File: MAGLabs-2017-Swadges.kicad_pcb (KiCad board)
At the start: 2 copper layers, 70 x 120 mm, 34 parts, among them J1 LCD Screen, J2 Valve Magic, J3 Program, U1 ESP12E

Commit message: Update design
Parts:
- moved C3 44.6 mm to (128.5, 38.0), turned to 270 degrees
- moved C4 37.7 mm to (153.0, 109.8)
- moved C2 25.3 mm to (118.6, 105.6), turned to 0 degrees
- moved R2 19.6 mm to (124.4, 107.6)
- moved R3 6.45 mm to (148.4, 112.0)
- moved C1 4.01 mm to (127.0, 82.8)
- moved R5 1.55 mm to (143.4, 112.0)
- moved R4 1.40 mm to (145.1, 112.0)
- moved R6 1.25 mm to (146.8, 112.0)
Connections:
- R2 pad 2: (no net) -> Net-(R2-Pad2)
- R3 pad 2: (no net) -> GPIO0
- S8 pad 1: Net-(S8-Pad1) -> Net-(R2-Pad2)
- U1 pad 17: Net-(S8-Pad1) -> Net-(R2-Pad2)
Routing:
- net Net-(BT1-Pad2): track 81.7 -> 165.8 mm
- net Net-(R2-Pad2): track 0.00 -> 71.9 mm
- net Net-(S8-Pad1): track 67.0 -> 0.00 mm
- net +3V3: track 309.2 -> 366.6 mm, vias 2 -> 9
- net GND: track 366.9 -> 378.1 mm, vias 16 -> 18
- net Net-(R5-Pad2): track 20.1 -> 15.2 mm, vias 0 -> 2
- net Net-(D1-Pad2): track 35.3 -> 31.7 mm
- net Net-(R6-Pad2): track 41.2 -> 39.4 mm
- net GPIO0: track 110.6 -> 112.1 mm, vias 2 -> 3

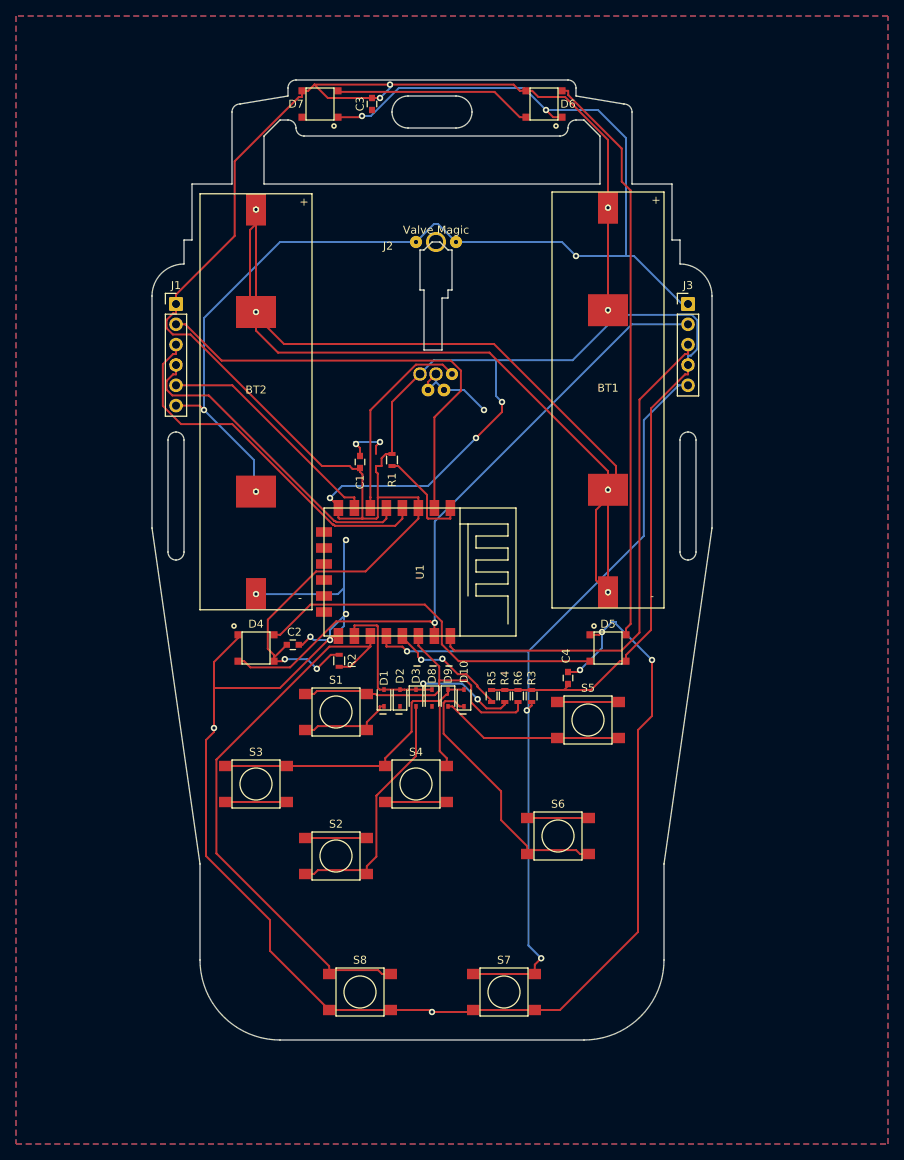
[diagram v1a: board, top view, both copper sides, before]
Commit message: Fixed diodes
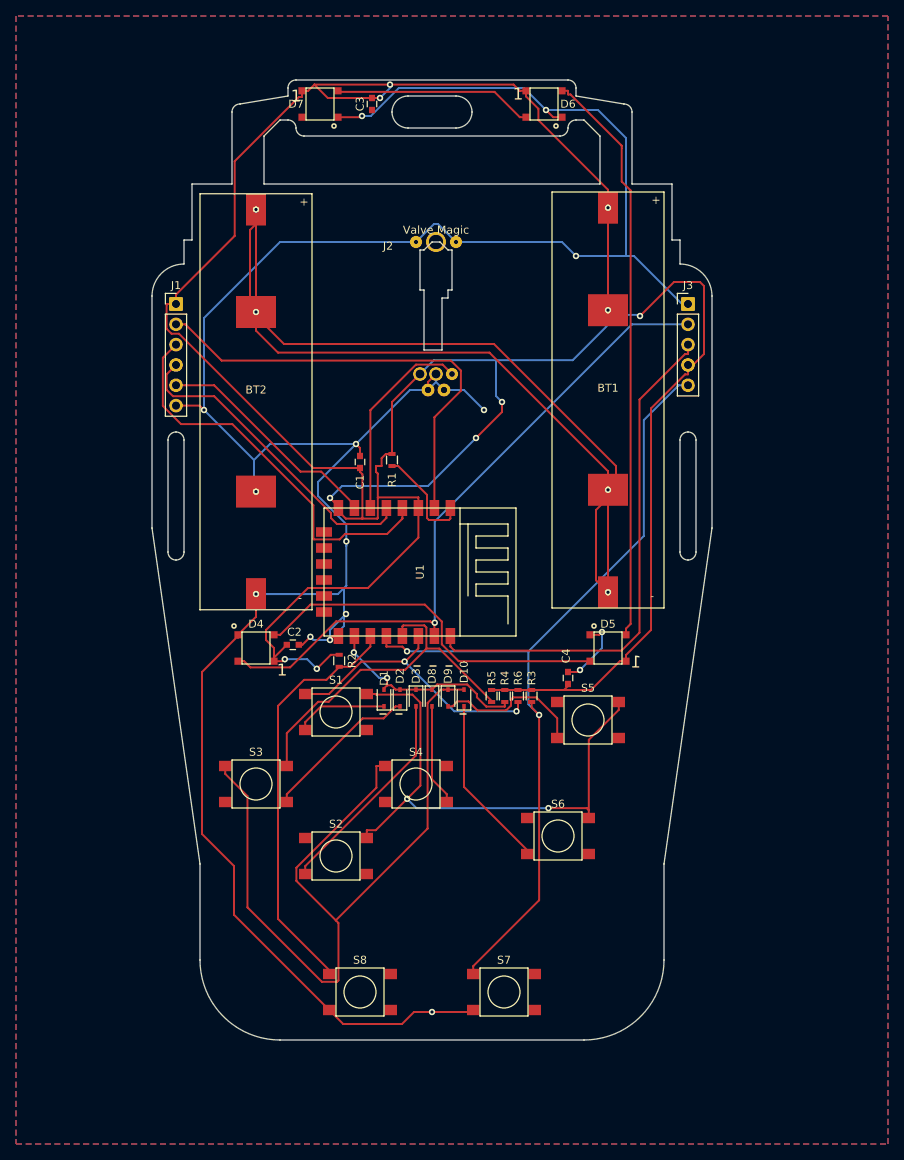
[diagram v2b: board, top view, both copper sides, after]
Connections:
- D2 pad 1: (no net) -> Net-(D2-Pad1)
- D7 pad 2: (no net) -> Net-(D7-Pad2)
- D8 pad 2: (no net) -> Net-(D8-Pad2)
- U1 pad 10: (no net) -> Net-(U1-Pad10)
- U1 pad 11: (no net) -> Net-(U1-Pad11)
- U1 pad 12: (no net) -> Net-(U1-Pad12)
- U1 pad 13: (no net) -> Net-(U1-Pad13)
- U1 pad 14: (no net) -> Net-(U1-Pad14)
- U1 pad 9: (no net) -> Net-(U1-Pad9)
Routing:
- net Net-(S1-Pad2): track 0.00 -> 67.2 mm, vias 0 -> 2
- net Net-(D10-Pad2): track 45.4 -> 105.5 mm
- net GND: track 378.1 -> 336.0 mm, vias 18 -> 15
- net Net-(R5-Pad2): track 15.2 -> 44.1 mm, vias 2 -> 0
- net Net-(R2-Pad2): track 71.9 -> 52.1 mm
- net Net-(D2-Pad1): track 0.00 -> 19.7 mm
- net Net-(D8-Pad2): track 0.00 -> 12.7 mm
- net Net-(D10-Pad1): track 34.0 -> 21.7 mm
- net Net-(S6-Pad1): track 7.70 -> 0.00 mm
- net Net-(S5-Pad1): track 7.70 -> 0.00 mm
- net Net-(S4-Pad3): track 7.70 -> 0.00 mm
- net Net-(S3-Pad3): track 7.70 -> 0.00 mm
- net Net-(S2-Pad1): track 7.70 -> 0.00 mm
- net +3V3: track 366.6 -> 372.6 mm, vias 9 -> 10
- net Net-(D1-Pad2): track 31.7 -> 26.3 mm
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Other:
- net class Default: clearance 0.2 -> 0.196
- rule trace_clearance: 0.2 -> 0.196
- board text added: "1"

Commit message: Update design
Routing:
- net GND: track 336.0 -> 373.8 mm, vias 15 -> 19
- net (no net): track 0.00 -> 1.51 mm
- net Net-(BT1-Pad2): track 165.8 -> 167.3 mm
- net +3V3: track 372.6 -> 371.8 mm

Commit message: Added button labels
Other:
- board text added: "A"
- board text added: "B"
- board text added: "LCD Screen"
- board text added: "Program"
- board text added: "SELECT"
- board text added: "START/PROGRAM"
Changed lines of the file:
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@@
-(kicad_pcb (version 4) (host pcbnew 4.0.6-e0-6349~53~ubuntu16.04.1)
+(kicad_pcb (version 20170123) (host pcbnew "(2017-07-14 revision d3b382c28)-master")
   (general
-    (links 80)
-    (no_connects 0)
-    (area 84 27 193.000001 168.000001)
     (thickness 1.6)
-    (drawings 88)
+    (drawings 107)
     (tracks 519)
     (zones 0)
@@
     (47 F.CrtYd user)
     (48 B.Fab user)
-    (49 F.Fab user hide)
+    (49 F.Fab user)
   )
   (setup
@@
     (visible_elements FFFFEFFF)
     (pcbplotparams
-      (layerselection 0x010f8_80000001)
+      (layerselection 0x010f8_ffffffff)
       (usegerberextensions true)
       (excludeedgelayer true)
@@
       (hpglpenspeed 20)
       (hpglpendiameter 15)
-      (hpglpenoverlay 2)
       (psnegative false)
       (psa4output false)
@@
     (at 145 149)
     (attr smd)
-    (fp_text reference S7 (at 0 -4) (layer F.SilkS)
+    (fp_text reference S7 (at 0 4) (layer F.SilkS)
       (effects (font (size 1 1) (thickness 0.15)))
     )
@@
     (at 127 149)
     (attr smd)
-    (fp_text reference S8 (at 0 -4) (layer F.SilkS)
+    (fp_text reference S8 (at 0 4) (layer F.SilkS)
       (effects (font (size 1 1) (thickness 0.15)))
     )
@@
     (at 124 132)
     (attr smd)
-    (fp_text reference S2 (at 0 -4) (layer F.SilkS)
+    (fp_text reference S2 (at 0 4) (layer F.SilkS)
       (effects (font (size 1 1) (thickness 0.15)))
     )
@@
       (effects (font (size 1 1) (thickness 0.15)))
     )
-    (fp_text value 0.1u (at -1.75 2.25 360) (layer F.Fab)
+    (fp_text value 0.1u (at -1.75 2.25) (layer F.Fab)
       (effects (font (size 1 1) (thickness 0.15)))
     )
@@
     )
   )
+  (gr_text Program (at 170 68 90) (layer F.SilkS)
+    (effects (font (size 1 1) (thickness 0.2)))
+  )
+  (gr_text "LCD Screen" (at 102 69.5 90) (layer F.SilkS)
+    (effects (font (size 1 1) (thickness 0.2)))
+  )
+  (gr_text A (at 155.5 120) (layer F.SilkS)
+    (effects (font (size 3 3) (thickness 0.3)))
+  )
+  (gr_text B (at 152 135) (layer F.SilkS)
+    (effects (font (size 3 3) (thickness 0.3)))
+  )
+  (gr_text START/PROGRAM (at 145 144) (layer F.SilkS)
+    (effects (font (size 1.5 1.5) (thickness 0.3)))
+  )
+  (gr_text SELECT (at 127 144) (layer F.SilkS)
+    (effects (font (size 1.5 1.5) (thickness 0.3)))
+  )
+  (gr_line (start 120 125) (end 118 123) (angle 90) (layer F.SilkS) (width 0.2))
+  (gr_line (start 120 124) (end 120 125) (angle 90) (layer F.SilkS) (width 0.2))
+  (gr_line (start 120 121) (end 120 124) (angle 90) (layer F.SilkS) (width 0.2))
+  (gr_line (start 118 123) (end 120 121) (angle 90) (layer F.SilkS) (width 0.2))
+  (gr_line (start 126 126) (end 124 128) (angle 90) (layer F.SilkS) (width 0.2))
+  (gr_line (start 122 126) (end 126 126) (angle 90) (layer F.SilkS) (width 0.2))
+  (gr_line (start 124 128) (end 122 126) (angle 90) (layer F.SilkS) (width 0.2))
+  (gr_line (start 128 125) (end 130 123) (angle 90) (layer F.SilkS) (width 0.2))
+  (gr_line (start 128 121) (end 128 125) (angle 90) (layer F.SilkS) (width 0.2))
+  (gr_line (start 130 123) (end 128 121) (angle 90) (layer F.SilkS) (width 0.2))
+  (gr_line (start 126 120) (end 124 118) (angle 90) (layer F.SilkS) (width 0.2))
+  (gr_line (start 122 120) (end 126 120) (angle 90) (layer F.SilkS) (width 0.2))
+  (gr_line (start 124 118) (end 122 120) (angle 90) (layer F.SilkS) (width 0.2))
   (gr_text 1 (at 146.75 36.75) (layer F.SilkS)
     (effects (font (size 1.5 1.5) (thickness 0.3)))

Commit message: Updates
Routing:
- net +3V3: track 371.8 -> 374.2 mm
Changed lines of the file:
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@@
     (thickness 1.6)
     (drawings 107)
-    (tracks 519)
+    (tracks 518)
     (zones 0)
     (modules 34)
@@
   (segment (start 159 85.225) (end 158 86.225) (width 0.25) (layer F.Cu) (net 1))
   (segment (start 114 64) (end 114 64.5) (width 0.25) (layer F.Cu) (net 1))
+  (segment (start 158 50.965) (end 158 42.5) (width 0.25) (layer F.Cu) (net 2) (status 400000))
+  (segment (start 148.9 37.5) (end 147.75 36.35) (width 0.25) (layer F.Cu) (net 2) (status 800000))
+  (segment (start 153 37.5) (end 148.9 37.5) (width 0.25) (layer F.Cu) (net 2))
+  (segment (start 158 42.5) (end 153 37.5) (width 0.25) (layer F.Cu) (net 2))
   (segment (start 146.49996 35.87496) (end 131.340125 35.87496) (width 0.25) (layer F.Cu) (net 2))
+  (segment (start 146.975 36.35) (end 146.49996 35.87496) (width 0.25) (layer F.Cu) (net 2))
+  (segment (start 131.340125 35.87496) (end 130.77444 35.87496) (width 0.25) (layer F.Cu) (net 2))
   (segment (start 147.75 36.35) (end 146.975 36.35) (width 0.25) (layer F.Cu) (net 2))
   (segment (start 129.5 37.25) (end 130.77444 35.97556) (width 0.25) (layer B.Cu) (net 2))
   (segment (start 130.77444 35.97556) (end 130.77444 35.87496) (width 0.25) (layer B.Cu) (net 2))
-  (segment (start 131.340125 35.87496) (end 130.77444 35.87496) (width 0.25) (layer F.Cu) (net 2))
   (segment (start 130.208755 35.87496) (end 130.77444 35.87496) (width 0.25) (layer F.Cu) (net 2))
   (via (at 130.77444 35.87496) (size 0.8) (drill 0.4) (layers F.Cu B.Cu) (net 2))
-  (segment (start 146.975 36.35) (end 146.49996 35.87496) (width 0.25) (layer F.Cu) (net 2))
   (segment (start 129.908495 35.5747) (end 130.208755 35.87496) (width 0.25) (layer F.Cu) (net 2))
   (segment (start 121.301 35.5747) (end 129.908495 35.5747) (width 0.25) (layer F.Cu) (net 2))
@@
   (segment (start 126.375 83.5) (end 127 83.5) (width 0.25) (layer F.Cu) (net 2))
   (segment (start 121.159002 83.5) (end 126.375 83.5) (width 0.25) (layer F.Cu) (net 2))
-  (segment (start 149.301 40.016) (end 158 48.715) (width 0.25) (layer F.Cu) (net 2))
-  (segment (start 149.301 38.601) (end 149.301 40.016) (width 0.25) (layer F.Cu) (net 2))
-  (segment (start 147.75 37.05) (end 149.301 38.601) (width 0.25) (layer F.Cu) (net 2))
-  (segment (start 158 48.715) (end 158 50.965) (width 0.25) (layer F.Cu) (net 2))
-  (segment (start 147.75 36.35) (end 147.75 37.05) (width 0.25) (layer F.Cu) (net 2))
   (via (at 121.6 108.6) (size 0.8) (layers F.Cu B.Cu) (net 2))
   (via (at 117.6 107.4) (size 0.8) (layers F.Cu B.Cu) (net 2))
@@
     (min_thickness 0.254)
     (keepout (tracks not_allowed) (vias not_allowed) (copperpour not_allowed))
-    (fill yes (arc_segments 16) (thermal_gap 0.508) (thermal_bridge_width 0.508))
+    (fill (arc_segments 16) (thermal_gap 0.508) (thermal_bridge_width 0.508))
     (polygon
       (pts
@@
     (min_thickness 0.254)
     (keepout (tracks not_allowed) (vias not_allowed) (copperpour not_allowed))
-    (fill yes (arc_segments 16) (thermal_gap 0.508) (thermal_bridge_width 0.508))
+    (fill (arc_segments 16) (thermal_gap 0.508) (thermal_bridge_width 0.508))
     (polygon
       (pts

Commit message: Pre route
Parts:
- added G1: LOGO, local:maglabs-backv2, B.Cu at (136.2, 90.8)
- added G2: LOGO, local:maglabs-frontv2, F.Cu at (136.0, 99.0)
- added R7: 10k, Resistors_SMD:R_0603, F.Cu at (148.2, 105.8)
- BT1, BT2: footprint local:BK-53 -> local:Elecrow-ThroughHole-AA-Battery
- J2: value Valve Magic -> IR Sensor; moved to B.Cu
- moved R1 32.9 mm to (154.2, 105.8)
- moved BT1 28.0 mm to (157.5, 103.0), turned to 90 degrees
- moved C1 26.5 mm to (140.2, 105.8)
- moved U1 25.8 mm to (150.5, 116.8)
- moved BT2 25.2 mm to (114.5, 50.0), turned to 270 degrees
- moved D1 23.8 mm to (106.5, 108.2)
- moved D10 23.8 mm to (116.5, 108.2)
- moved D2 23.8 mm to (108.5, 108.2)
- moved D3 23.8 mm to (110.5, 108.2)
- moved D8 23.8 mm to (112.5, 108.2)
- moved D9 23.8 mm to (114.5, 108.2)
- moved R4 18.3 mm to (127.0, 109.5)
- moved S5 15.9 mm to (159.0, 130.5)
- moved R3 15.7 mm to (133.0, 109.5)
- moved R6 15.5 mm to (131.5, 109.5)
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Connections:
- J1 pad 3: Net-(J1-Pad3) -> Net-(D1-Pad2)
- R4 pad 1: +3V3 -> GND
- R4 pad 2: Net-(D1-Pad2) -> Net-(R4-Pad2)
- U1 pad 16: Net-(D1-Pad2) -> Net-(R4-Pad2)
- U1 pad 4: Net-(J1-Pad3) -> Net-(D1-Pad2)
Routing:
- net +3V3: track 374.2 -> 0.00 mm, vias 10 -> 0
- net GND: track 373.8 -> 0.00 mm, vias 19 -> 0
- net Net-(BT1-Pad2): track 167.3 -> 0.00 mm, vias 4 -> 0
- net GPIO0: track 107.8 -> 0.00 mm, vias 2 -> 0
- net Net-(D10-Pad2): track 105.5 -> 2.00 mm
- net RXD: track 83.6 -> 0.00 mm, vias 1 -> 0
- net Net-(D5-Pad2): track 72.3 -> 0.00 mm
- net Net-(S1-Pad2): track 67.2 -> 0.00 mm, vias 2 -> 0
- net TXD: track 64.8 -> 0.00 mm
- net Net-(J1-Pad2): track 56.6 -> 0.00 mm
- net Net-(R2-Pad2): track 52.1 -> 0.00 mm
- net Net-(J1-Pad3): track 50.1 -> 0.00 mm
- net Net-(D4-Pad2): track 45.7 -> 0.00 mm
- net Net-(R5-Pad2): track 44.1 -> 0.00 mm
- net Net-(J1-Pad4): track 39.9 -> 0.00 mm
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- removed copper zone on B.Cu, net GND
- removed copper zone on F.Cu, net GND
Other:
- outline, holes or cut-outs redrawn
- board text removed: "1"

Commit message: Should be good?
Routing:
- net GND: track 0.00 -> 460.9 mm, vias 0 -> 13
- net +3V3: track 0.00 -> 235.9 mm
- net Net-(S1-Pad2): track 0.00 -> 111.0 mm
- net GPIO0: track 0.00 -> 102.1 mm
- net Net-(D9-Pad2): track 0.00 -> 97.8 mm
- net Net-(D10-Pad1): track 0.00 -> 87.1 mm
- net RXD: track 0.00 -> 83.1 mm
- net Net-(D1-Pad2): track 6.00 -> 88.6 mm
- net Net-(J1-Pad2): track 0.00 -> 78.8 mm, vias 0 -> 1
- net Net-(D5-Pad2): track 0.00 -> 74.9 mm
- net Net-(J2-Pad3): track 0.00 -> 65.5 mm
- net Net-(J1-Pad4): track 0.00 -> 60.0 mm
- net Net-(R2-Pad2): track 0.00 -> 56.3 mm
- net Net-(J1-Pad5): track 0.00 -> 53.2 mm
- net Net-(BT1-Pad2): track 0.00 -> 50.2 mm
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- added copper zone on B.Cu, net GND
- added copper zone on F.Cu, net GND
